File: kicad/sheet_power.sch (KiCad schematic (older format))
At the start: 24 parts, among them SW58 SW_POWER, U4 BQ24072RGTR, U5 AP2210-33

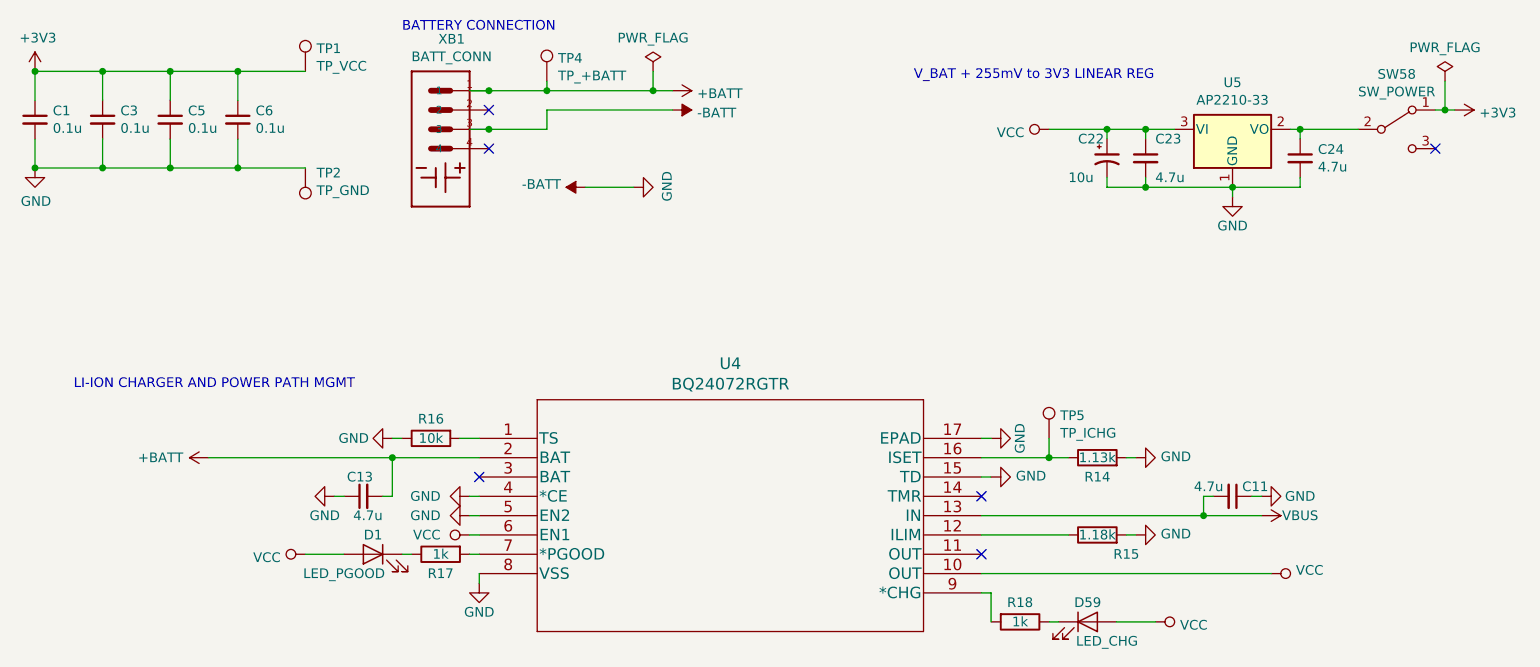
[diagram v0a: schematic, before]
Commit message: kicad: completed partial layout
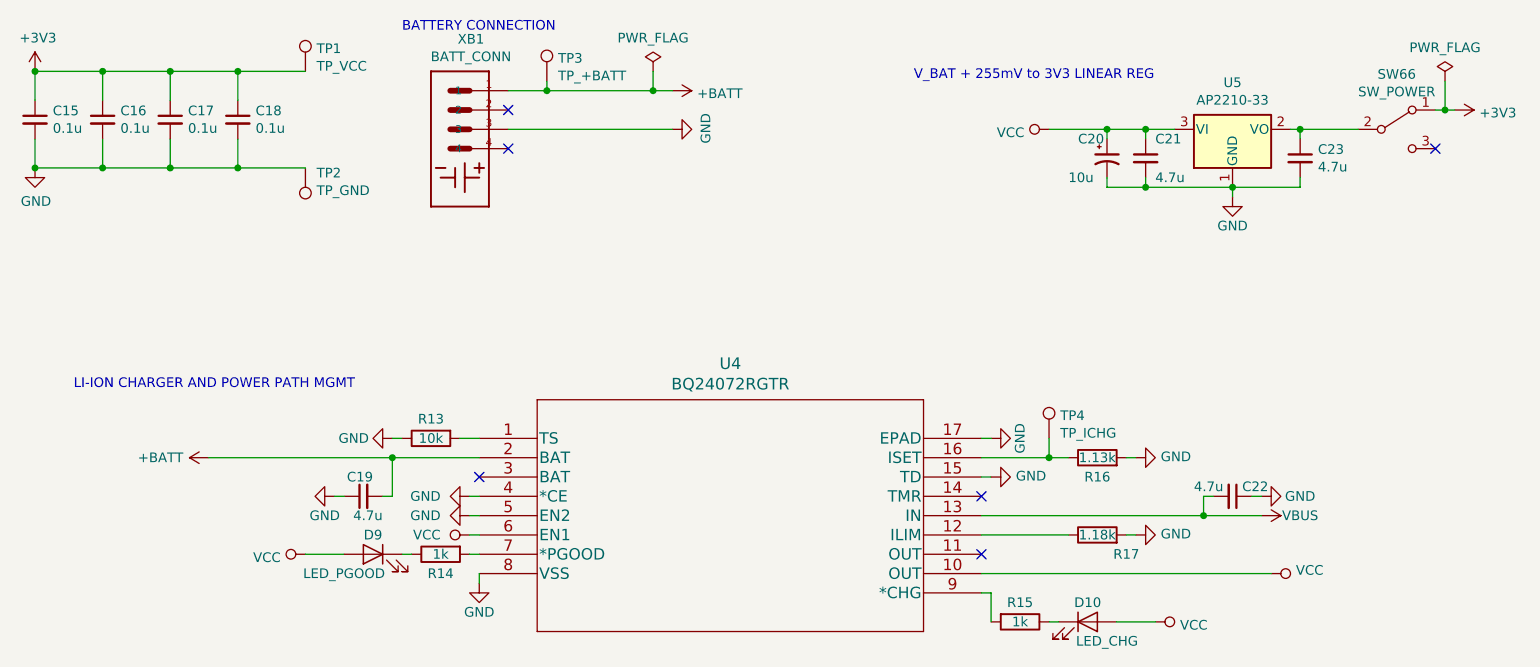
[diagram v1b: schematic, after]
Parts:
- renumbered C1 to C15, C3 to C16, C5 to C17, C6 to C18, C13 to C19, C22 to C20, C23 to C21, C11 to C22, C24 to C23, D59 to D10, D1 to D9, R16 to R13, R17 to R14, R18 to R15, R14 to R16, R15 to R17, SW58 to SW66, TP4 to TP3, TP5 to TP4
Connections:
- net -BATT renamed GND
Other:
- moved on the sheet: XB1

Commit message: kicad: finalize device BOM
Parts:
- C15, C16, C17, C18: Description (none) -> Assorted display; Digi-Key PN (none) -> 1276-1005-1-ND; Digi-Key Page (none) -> https://www.digikey.com/product-detail/en/samsung-electro-m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
- C19, C21, C22, C23: Description (none) -> USB power decoupling; Digi-Key PN (none) -> 1276-1045-1-ND; Digi-Key Page (none) -> https://www.digikey.com/product-detail/en/samsung-electro-m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
- C20: Description (none) -> Power decoupling; Digi-Key PN (none) -> 493-10106-1-ND; Digi-Key Page (none) -> https://www.digikey.com/product-detail/en/nichicon/UZR1C100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
- D10, D9: Description (none) -> Indicator LED; Digi-Key PN (none) -> SML-D12U1WT86CT-ND; Digi-Key Page (none) -> https://www.digikey.com/product-detail/en/rohm-semiconducto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
- R13: Description (none) -> Input pull-down resistor; Digi-Key PN (none) -> 311-10.0KHRCT-ND; Digi-Key Page (none) -> https://www.digikey.com/product-detail/en/yageo/RC0603FR-07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
- R14, R15: Description (none) -> LED current limiting; Digi-Key PN (none) -> 311-1.00KHRCT-ND; Digi-Key Page (none) -> https://www.digikey.com/product-detail/en/yageo/RC0603FR-07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
- R16: Description (none) -> Battery Management ISET; Digi-Key PN (none) -> 311-1.13KHRCT-ND; Digi-Key Page (none) -> https://www.digikey.com/product-detail/en/yageo/RC0603FR-07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
- R17: Description (none) -> Battery Management ILIM; Digi-Key PN (none) -> 311-1.18KHRCT-ND; Digi-Key Page (none) -> https://www.digikey.com/product-detail/en/yageo/RC0603FR-07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
- SW66: Description (none) -> Power switch; Digi-Key PN (none) -> 401-1999-1-ND; Digi-Key Page (none) -> https://www.digikey.com/product-detail/en/c-k/JS102011SAQN/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
- U4: Description (none) -> IC LI-ION Charge Mgmt; Digi-Key PN (none) -> 296-38871-1-ND; Digi-Key Page (none) -> https://www.digikey.com/product-detail/en/texas-instruments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
- U5: Description (none) -> Linear Voltage Reg IC Positive Fixed 1 Output 300mA; Digi-Key PN (none) -> AP2210N-3.3TRG1DICT-ND; Digi-Key Page (none) -> https://www.digikey.com/product-detail/en/diodes-incorporat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
- XB1: Description (none) -> Right Angle SMT Battery Conn; Digi-Key PN (none) -> 478-5452-1-ND; Digi-Key Page (none) -> https://www.digikey.com/product-detail/en/avx-corporation/0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

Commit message: kicad: fix virtual component
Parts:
- C15, C16, C17, C18: part_num (none) -> CL10B104KO8NNNC
- C19, C21, C22, C23: part_num (none) -> CL10A475KQ8NNNC
- C20: part_num (none) -> UZR1C100MCL1GB
- D10, D9: part_num (none) -> SML-D12U1WT86
- R13: part_num (none) -> RC0603FR-0710KL
- R14, R15: part_num (none) -> RC0603FR-071KL
- R16: part_num (none) -> RC0603FR-071K13L
- R17: part_num (none) -> RC0603FR-071K18L
- SW66: part_num (none) -> JS102011SAQN
- U4: part_num (none) -> BQ24072RGTR
- U5: part_num (none) -> AP2210N-3.3TRG1
- XB1: part_num (none) -> 009155004541006
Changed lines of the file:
@@
 F 5 "1276-1005-1-ND" H 900 1100 50  0001 C CNN "Digi-Key PN"
 F 6 "https://www.digikey.com/product-detail/en/samsung-electro-mechanics/CL10B104KO8NNNC/1276-1005-1-ND/3889091" H 900 1100 50  0001 C CNN "Digi-Key Page"
+F 7 "CL10B104KO8NNNC" H 900 1100 50  0001 C CNN "part_num"
 	1    900  1100
 	1    0    0    -1
@@
 F 5 "1276-1005-1-ND" H 1250 1100 50  0001 C CNN "Digi-Key PN"
 F 6 "https://www.digikey.com/product-detail/en/samsung-electro-mechanics/CL10B104KO8NNNC/1276-1005-1-ND/3889091" H 1250 1100 50  0001 C CNN "Digi-Key Page"
+F 7 "CL10B104KO8NNNC" H 1250 1100 50  0001 C CNN "part_num"
 	1    1250 1100
 	1    0    0    -1
@@
 F 5 "1276-1005-1-ND" H 1600 1100 50  0001 C CNN "Digi-Key PN"
 F 6 "https://www.digikey.com/product-detail/en/samsung-electro-mechanics/CL10B104KO8NNNC/1276-1005-1-ND/3889091" H 1600 1100 50  0001 C CNN "Digi-Key Page"
+F 7 "CL10B104KO8NNNC" H 1600 1100 50  0001 C CNN "part_num"
 	1    1600 1100
 	1    0    0    -1
@@
 F 5 "1276-1005-1-ND" H 1950 1100 50  0001 C CNN "Digi-Key PN"
 F 6 "https://www.digikey.com/product-detail/en/samsung-electro-mechanics/CL10B104KO8NNNC/1276-1005-1-ND/3889091" H 1950 1100 50  0001 C CNN "Digi-Key Page"
+F 7 "CL10B104KO8NNNC" H 1950 1100 50  0001 C CNN "part_num"
 	1    1950 1100
 	1    0    0    -1
@@
 F 5 "311-10.0KHRCT-ND" H 2950 2750 50  0001 C CNN "Digi-Key PN"
 F 6 "https://www.digikey.com/product-detail/en/yageo/RC0603FR-0710KL/311-10.0KHRCT-ND/729827" H 2950 2750 50  0001 C CNN "Digi-Key Page"
+F 7 "RC0603FR-0710KL" H 2950 2750 50  0001 C CNN "part_num"
 	1    2950 2750
 	0    -1   1    0
@@
 F 5 "311-1.18KHRCT-ND" H 6400 3250 50  0001 C CNN "Digi-Key PN"
 F 6 "https://www.digikey.com/product-detail/en/yageo/RC0603FR-071K18L/311-1.18KHRCT-ND/729798" H 6400 3250 50  0001 C CNN "Digi-Key Page"
+F 7 "RC0603FR-071K18L" H 6400 3250 50  0001 C CNN "part_num"
 	1    6400 3250
 	0    -1   -1   0
@@
 F 5 "311-1.13KHRCT-ND" H 6400 2850 50  0001 C CNN "Digi-Key PN"
 F 6 "https://www.digikey.com/product-detail/en/yageo/RC0603FR-071K13L/311-1.13KHRCT-ND/729796" H 6400 2850 50  0001 C CNN "Digi-Key Page"
+F 7 "RC0603FR-071K13L" H 6400 2850 50  0001 C CNN "part_num"
 	1    6400 2850
 	0    -1   -1   0
@@
 F 5 "SML-D12U1WT86CT-ND" H 2650 3350 50  0001 C CNN "Digi-Key PN"
 F 6 "https://www.digikey.com/product-detail/en/rohm-semiconductor/SML-D12U1WT86/SML-D12U1WT86CT-ND/5843858" H 2650 3350 50  0001 C CNN "Digi-Key Page"
+F 7 "SML-D12U1WT86" H 2650 3350 50  0001 C CNN "part_num"
 	1    2650 3350
 	-1   0    0    -1
@@
 F 5 "311-1.00KHRCT-ND" H 3000 3350 50  0001 C CNN "Digi-Key PN"
 F 6 "https://www.digikey.com/product-detail/en/yageo/RC0603FR-071KL/311-1.00KHRCT-ND/729790" H 3000 3350 50  0001 C CNN "Digi-Key Page"
+F 7 "RC0603FR-071KL" H 3000 3350 50  0001 C CNN "part_num"
 	1    3000 3350
 	0    -1   1    0
@@
 F 5 "https://www.digikey.com/product-detail/en/samsung-electro-mechanics/CL10A475KQ8NNNC/1276-1045-1-ND/3889131" H 7100 3050 50  0001 C CNN "Digi-Key Page"
 F 6 "1276-1045-1-ND" H 7100 3050 50  0001 C CNN "Digi-Key PN"
+F 7 "CL10A475KQ8NNNC" H 7100 3050 50  0001 C CNN "part_num"
 	1    7100 3050
 	0    1    1    0
@@
 F 5 "311-1.00KHRCT-ND" H 6000 3700 50  0001 C CNN "Digi-Key PN"
 F 6 "https://www.digikey.com/product-detail/en/yageo/RC0603FR-071KL/311-1.00KHRCT-ND/729790" H 6000 3700 50  0001 C CNN "Digi-Key Page"
+F 7 "RC0603FR-071KL" H 6000 3700 50  0001 C CNN "part_num"
 	1    6000 3700
 	0    1    1    0
@@
 F 5 "SML-D12U1WT86CT-ND" H 6350 3700 50  0001 C CNN "Digi-Key PN"
 F 6 "https://www.digikey.com/product-detail/en/rohm-semiconductor/SML-D12U1WT86/SML-D12U1WT86CT-ND/5843858" H 6350 3700 50  0001 C CNN "Digi-Key Page"
+F 7 "SML-D12U1WT86" H 6350 3700 50  0001 C CNN "part_num"
 	1    6350 3700
 	1    0    0    -1
@@
 F 5 "AP2210N-3.3TRG1DICT-ND" H 7100 1150 50  0001 C CNN "Digi-Key PN"
 F 6 "https://www.digikey.com/product-detail/en/diodes-incorporated/AP2210N-3.3TRG1/AP2210N-3.3TRG1DICT-ND/4505294" H 7100 1150 50  0001 C CNN "Digi-Key Page"
+F 7 "AP2210N-3.3TRG1" H 7100 1150 50  0001 C CNN "part_num"
 	1    7100 1150
 	1    0    0    -1
@@
 F 5 "https://www.digikey.com/product-detail/en/samsung-electro-mechanics/CL10A475KQ8NNNC/1276-1045-1-ND/3889131" H 6650 1300 50  0001 C CNN "Digi-Key Page"
 F 6 "1276-1045-1-ND" H 6650 1300 50  0001 C CNN "Digi-Key PN"
+F 7 "CL10A475KQ8NNNC" H 6650 1300 50  0001 C CNN "part_num"
 	1    6650 1300
 	1    0    0    -1
@@
 F 5 "https://www.digikey.com/product-detail/en/samsung-electro-mechanics/CL10A475KQ8NNNC/1276-1045-1-ND/3889131" H 7450 1300 50  0001 C CNN "Digi-Key Page"
 F 6 "1276-1045-1-ND" H 7450 1300 50  0001 C CNN "Digi-Key PN"
+F 7 "CL10A475KQ8NNNC" H 7450 1300 50  0001 C CNN "part_num"
 	1    7450 1300
 	1    0    0    -1
@@
 F 5 "493-10106-1-ND" H 6450 1300 50  0001 C CNN "Digi-Key PN"
 F 6 "https://www.digikey.com/product-detail/en/nichicon/UZR1C100MCL1GB/493-10106-1-ND/3983951" H 6450 1300 50  0001 C CNN "Digi-Key Page"
+F 7 "UZR1C100MCL1GB" H 6450 1300 50  0001 C CNN "part_num"
 	1    6450 1300
 	1    0    0    -1
@@
 F 5 "296-38871-1-ND" H 3200 2750 50  0001 C CNN "Digi-Key PN"
 F 6 "https://www.digikey.com/product-detail/en/texas-instruments/BQ24072RGTR/296-38871-1-ND/5142983" H 3200 2750 50  0001 C CNN "Digi-Key Page"
+F 7 "BQ24072RGTR" H 3200 2750 50  0001 C CNN "part_num"
 	1    3200 2750
 	1    0    0    -1
@@
 F 5 "https://www.digikey.com/product-detail/en/samsung-electro-mechanics/CL10A475KQ8NNNC/1276-1045-1-ND/3889131" H 2600 3050 50  0001 C CNN "Digi-Key Page"
 F 6 "1276-1045-1-ND" H 2600 3050 50  0001 C CNN "Digi-Key PN"
+F 7 "CL10A475KQ8NNNC" H 2600 3050 50  0001 C CNN "part_num"
 	1    2600 3050
 	0    -1   1    0
@@
 F 5 "401-1999-1-ND" H 7950 1150 50  0001 C CNN "Digi-Key PN"
 F 6 "https://www.digikey.com/product-detail/en/c-k/JS102011SAQN/401-1999-1-ND/1640114" H 7950 1150 50  0001 C CNN "Digi-Key Page"
+F 7 "JS102011SAQN" H 7950 1150 50  0001 C CNN "part_num"
 	1    7950 1150
 	1    0    0    -1
@@
 F 10 "478-5452-1-ND" H 3100 1100 50  0001 C CNN "Digi-Key PN"
 F 11 "https://www.digikey.com/product-detail/en/avx-corporation/009155004541006/478-5452-1-ND/2001013" H 3100 1100 50  0001 C CNN "Digi-Key Page"
+F 12 "009155004541006" H 3100 1100 50  0001 C CNN "part_num"
 	1    3100 1100
 	-1   0    0    -1
